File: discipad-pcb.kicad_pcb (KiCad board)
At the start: 2 copper layers, 76.3 x 122.8 mm, 63 parts, among them J1 AVR-ISP-6, SW0 KEYSW, SW1 KEYSW, SW10 KEYSW, SW11 KEYSW, SW12 KEYSW, SW13 KEYSW, SW14 KEYSW, SW15 KEYSW, SW16 KEYSW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

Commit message: version update
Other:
- net class Default removed

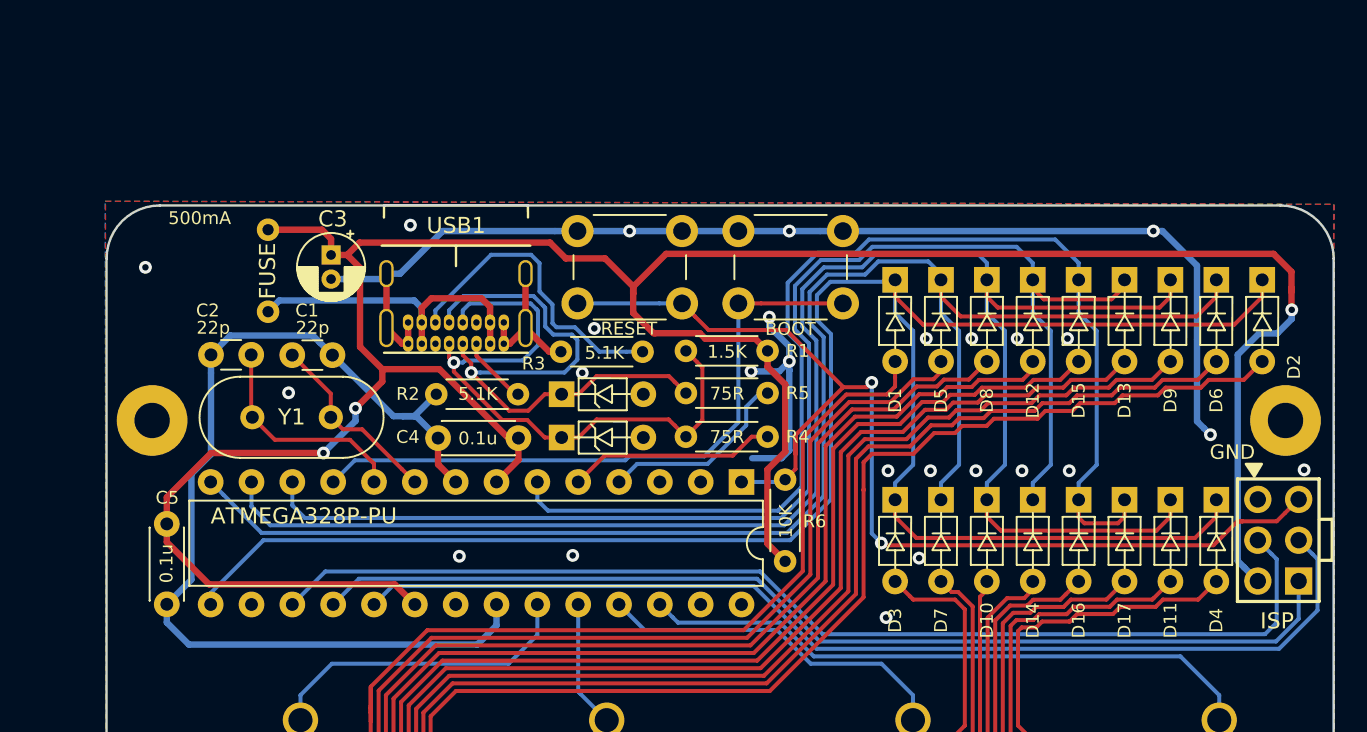
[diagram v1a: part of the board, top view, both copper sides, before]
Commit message: pulled new footprint to pcb
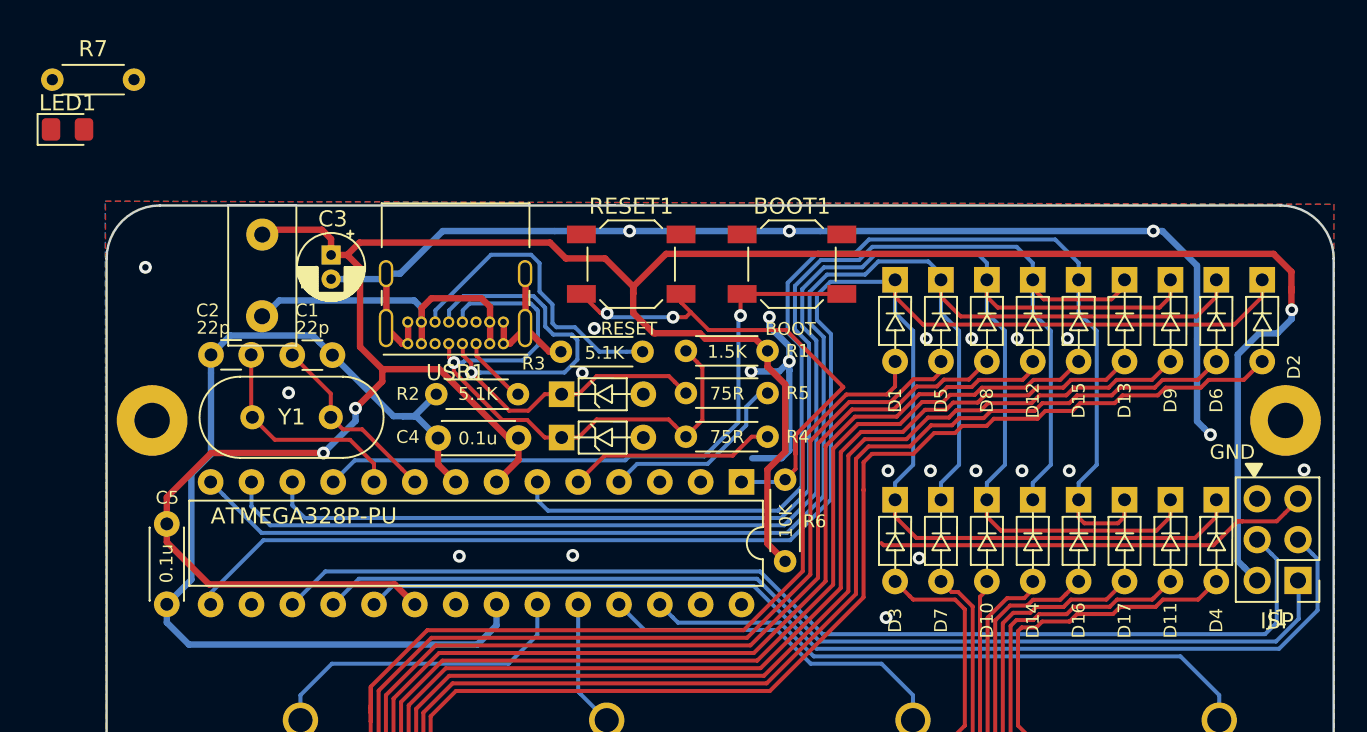
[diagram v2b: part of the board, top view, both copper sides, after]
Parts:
- added LED1: POWER, LED_SMD:LED_0805_2012Metric_Pad1.15x1.40mm_HandSolder, F.Cu at (103.2, 10.4)
- added R7: 1.5K, Resistor_THT:R_Axial_DIN0204_L3.6mm_D1.6mm_P5.08mm_Horizontal, F.Cu at (102.3, 7.28)
- BOOT1, RESET1: footprint Button_Switch_THT:SW_PUSH_6mm -> Button_Switch_SMD:SW_SPST_SKQG_WithStem
- F1: footprint keyboard_parts:polyfuse_5.1mm -> Fuse:Fuse_Littelfuse_395Series
- J1: footprint keyboard_parts:AVR_ICSP_3x2 -> Connector_PinHeader_2.54mm:PinHeader_2x03_P2.54mm_Vertical
- USB1: footprint Type-C:USB_C_GCT_USB4085 -> Connector_USB:USB_C_Receptacle_GCT_USB4085
- moved USB1 6.78 mm to (130.4, 23.7)
- moved RESET1 3.92 mm to (138.3, 18.8)
- moved BOOT1 3.92 mm to (148.3, 18.8)
- moved J1 2.79 mm to (179.8, 38.4), turned to 180 degrees
- moved F1 2.28 mm to (115.4, 16.9)
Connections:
- U1 pad 16: Net-(U1-Pad16) -> unconnected-(U1-Pad16)
- U1 pad 2: Net-(U1-Pad2) -> unconnected-(U1-Pad2)
- U1 pad 21: Net-(U1-Pad21) -> unconnected-(U1-Pad21)
- U1 pad 27: Net-(U1-Pad27) -> unconnected-(U1-Pad27)
- U1 pad 28: Net-(U1-Pad28) -> unconnected-(U1-Pad28)
- U1 pad 3: Net-(U1-Pad3) -> unconnected-(U1-Pad3)
- USB1 pad A8: Net-(USB1-PadA8) -> unconnected-(USB1-PadA8)
- USB1 pad B8: Net-(USB1-PadB8) -> unconnected-(USB1-PadB8)
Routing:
- net reset: track 70.2 -> 59.7 mm
- net boot: track 40.6 -> 41.0 mm, vias 0 -> 1
- net GND: vias 27 -> 26

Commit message: integrated power led to pcb
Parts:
- F1: footprint Fuse:Fuse_Littelfuse_395Series -> led:polyfuse_5.1mm
- moved LED1 71.4 mm to (171.6, 30.9), turned to 180 degrees
- moved R7 70.3 mm to (169.3, 28.6)
- moved F1 2.30 mm to (115.6, 19.2)
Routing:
- net GND: track 160.5 -> 146.0 mm
- net Net-(LED1-Pad2): track 0.00 -> 2.79 mm
- net +5V: track 174.6 -> 176.7 mm
